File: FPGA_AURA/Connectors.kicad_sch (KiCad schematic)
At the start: 10 parts, among them J700 SS5-40-3.50-X-D-K-XX, J701 SS5-20-3.50-X-D-K-XX

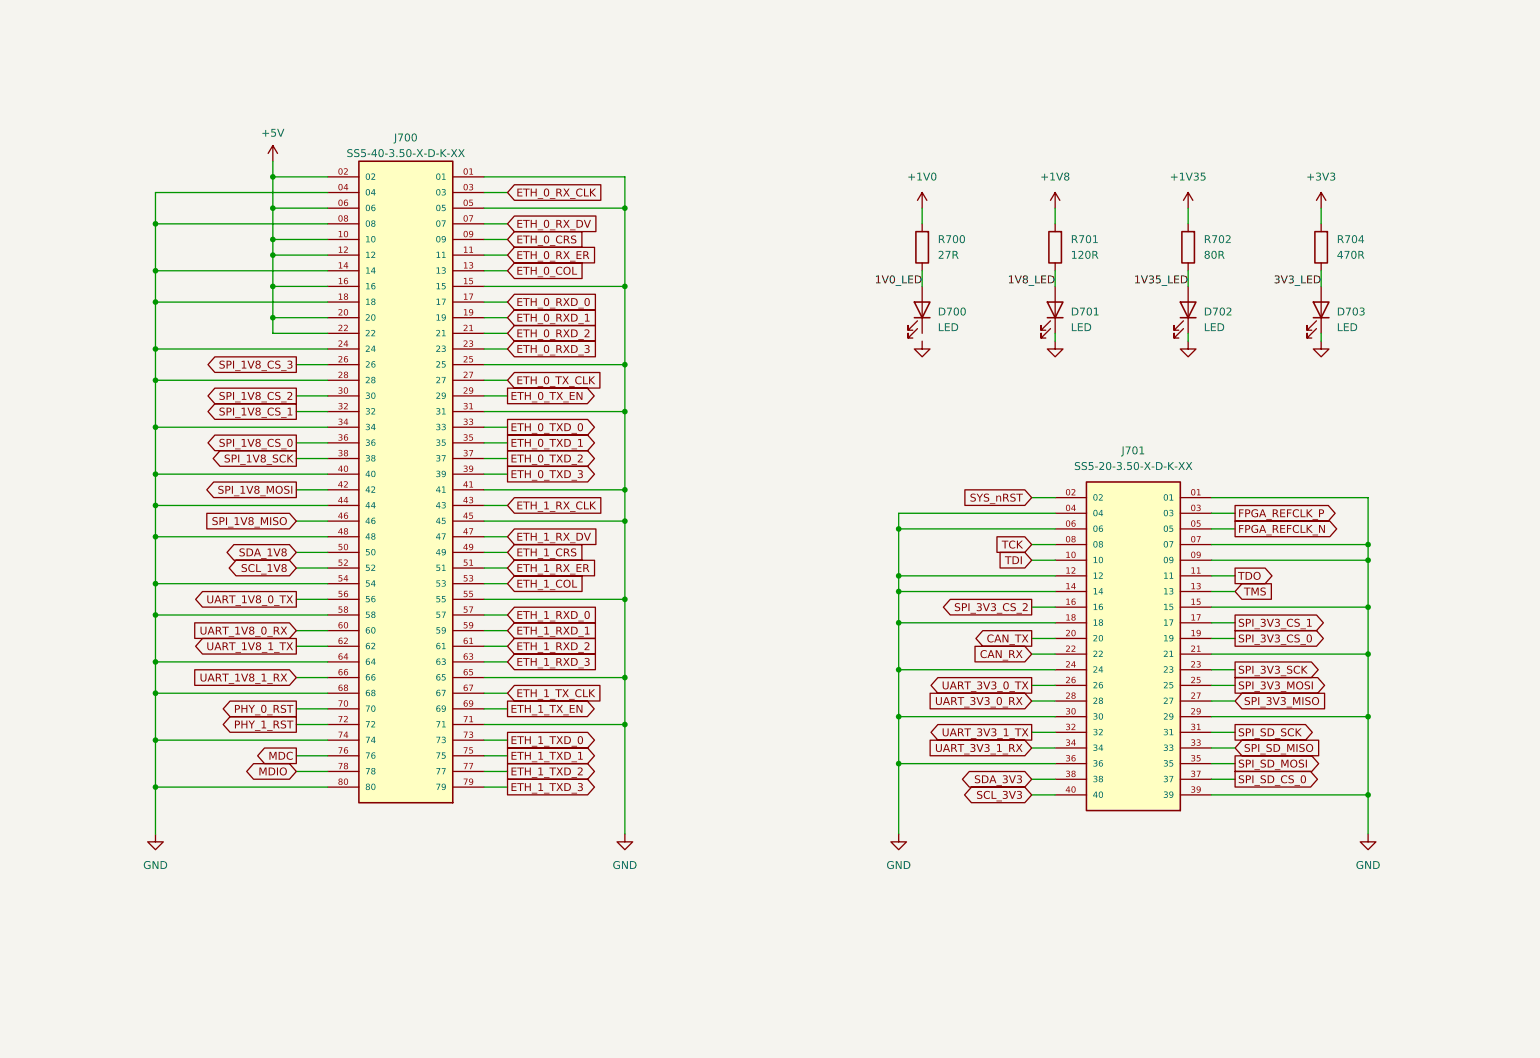
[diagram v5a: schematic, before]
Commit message: Schematic initial draft complete.
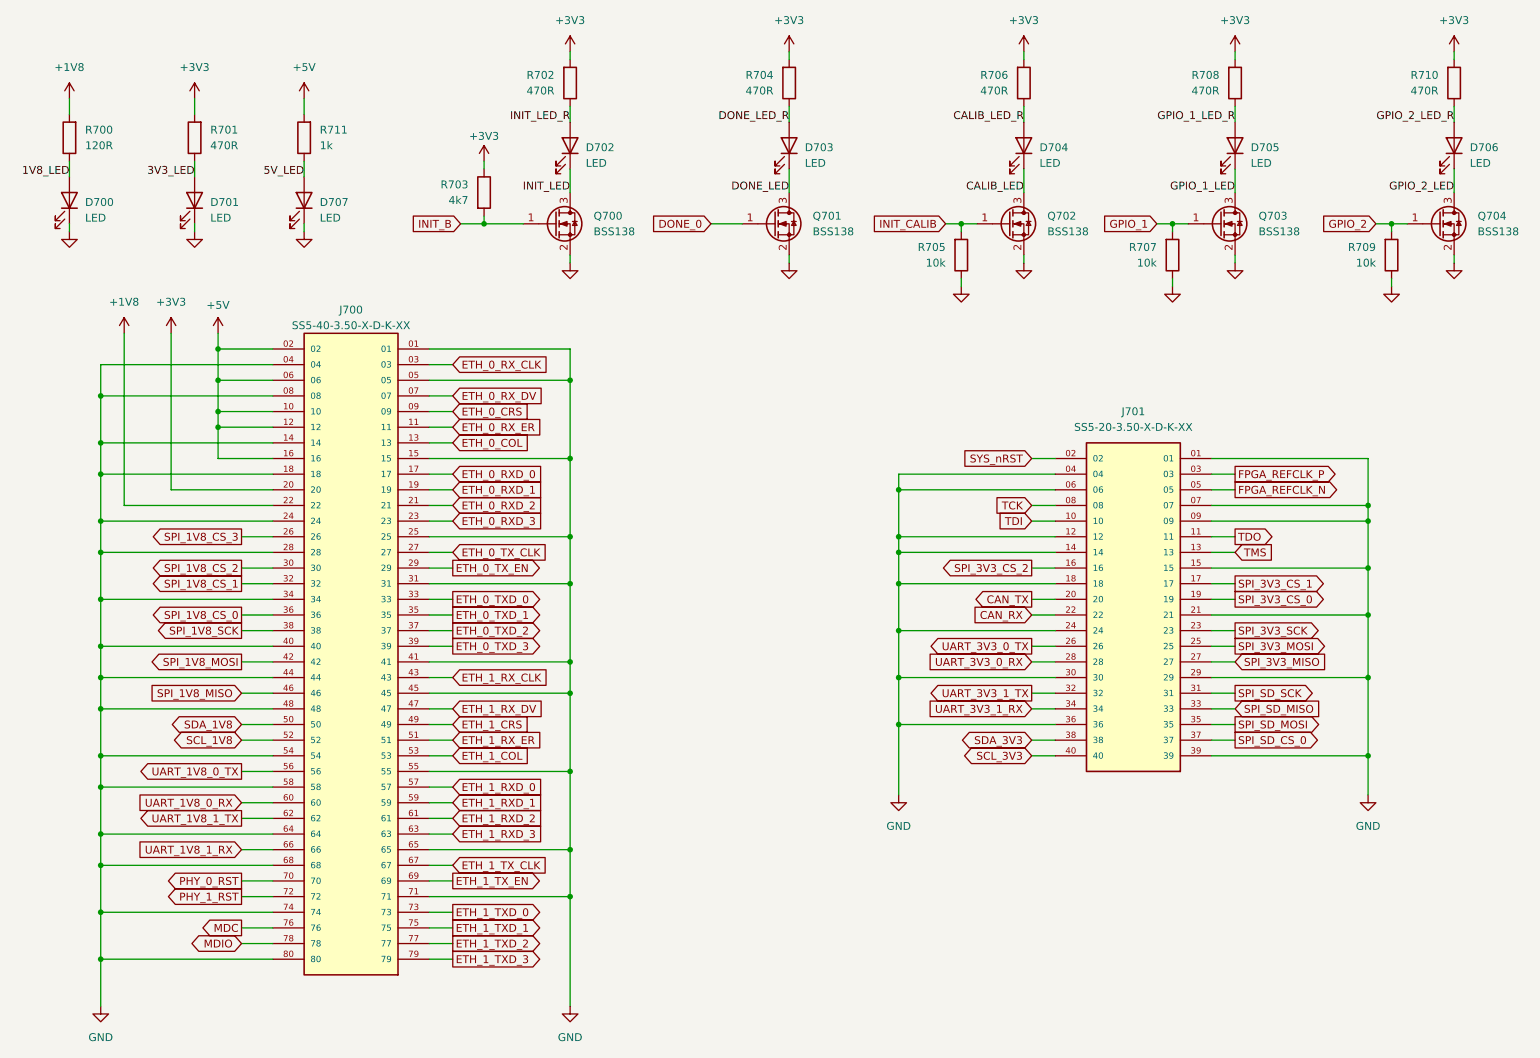
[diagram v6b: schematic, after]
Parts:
- removed D700: LED, LED_SMD:LED_0603_1608Metric, symbol Device:LED
- removed R700: 27R, Resistor_SMD:R_0402_1005Metric, symbol Device:R
- added D703, D704, D705, D706, D707: LED, LED_SMD:LED_0603_1608Metric, symbol Device:LED
- added Q700, Q701, Q702, Q703, Q704: BSS138, Package_TO_SOT_SMD:SOT-23, symbol Transistor_FET:BSS138
- added R703: 4k7, Resistor_SMD:R_0402_1005Metric, symbol Device:R
- added R704, R706, R708, R710: 470R, Resistor_SMD:R_0402_1005Metric, symbol Device:R
- added R705, R707, R709: 10k, Resistor_SMD:R_0402_1005Metric, symbol Device:R
- added R711: 1k, Resistor_SMD:R_0402_1005Metric, symbol Device:R
- R702: value 80R -> 470R
- renumbered D701 to D700, D703 to D701, R701 to R700, R704 to R701
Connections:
- net +1V35 is gone; now on net +3V3: R702.2
- net +1V8: now also J700.22
- net +3V3: now also J700.20, R703.1, R704.2, R706.2, R708.2, R710.2
- net +5V: now also R711.2; no longer J700.20, J700.22
- net GND: now also D707.1 (K), Q700.2 (S), Q701.2 (S), Q702.2 (S), Q703.2 (S), Q704.2 (S), R705.1, R707.1, R709.1; no longer D702.1 (K)
- net 1V35_LED renamed INIT_LED_R
- new net 5V_LED: D707.2 (A), R711.1
- new net CALIB_LED: D704.1 (K), Q702.3 (D)
- new net CALIB_LED_R: D704.2 (A), R706.1
- new net DONE_0: Q701.1 (G)
- new net DONE_LED: D703.1 (K), Q701.3 (D)
- new net DONE_LED_R: D703.2 (A), R704.1
- new net GPIO_1: Q703.1 (G), R707.2
- new net GPIO_1_LED: D705.1 (K), Q703.3 (D)
- new net GPIO_1_LED_R: D705.2 (A), R708.1
- new net GPIO_2: Q704.1 (G), R709.2
- new net GPIO_2_LED: D706.1 (K), Q704.3 (D)
- new net GPIO_2_LED_R: D706.2 (A), R710.1
- new net INIT_B: Q700.1 (G), R703.2
- new net INIT_CALIB: Q702.1 (G), R705.2
- new net INIT_LED: D702.1 (K), Q700.3 (D)
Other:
- moved on the sheet: D700, D701, J700, J701, R700, R701
